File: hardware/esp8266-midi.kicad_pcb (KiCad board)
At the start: 2 copper layers, 62.2 x 63.5 mm, 26 parts, among them J1 MIDI in, J2 MIDI out, J3 TTL-232R-3V3 connector, J4 Bat+, J5 Bat-, SW1 reset, SW2 Prog enable, U1 ESP-12F, U2 6N138, U3 LD1117S50TR_SOT223

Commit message: Initial rev of schematic and PCB, WIP
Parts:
- added C5: 220uF, Capacitors_THT:CP_Radial_D5.0mm_P2.50mm, F.Cu at (125.1, 122.6)
- D1: footprint Diodes_THT:D_DO-41_SOD81_P10.16mm_Horizontal -> Diodes_THT:D_A-405_P10.16mm_Horizontal
- R1, R3, R4, R6: footprint Resistors_THT:R_Axial_DIN0204_L3.6mm_D1.6mm_P7.62mm_Horizontal -> Resistors_THT:R_Axial_DIN0207_L6.3mm_D2.5mm_P10.16mm_Horizontal
- R2, R5: value 430R -> 220R; footprint Resistors_THT:R_Axial_DIN0204_L3.6mm_D1.6mm_P7.62mm_Horizontal -> Resistors_THT:R_Axial_DIN0207_L6.3mm_D2.5mm_P10.16mm_Horizontal
- SW2: value Prog enable -> prog enable
- moved SW1 17.9 mm to (153.0, 128.9), turned to 180 degrees
- moved mount 11.4 mm to (136.5, 84.5)
- moved SW2 10.2 mm to (135.9, 124.5)
- moved R2 3.56 mm to (138.4, 90.2)
- moved D1 1.55 mm to (124.5, 89.5)
- moved R4 1.53 mm to (114.3, 104.1), turned to 90 degrees
- moved R3 0.92 mm to (120.7, 104.1)
- moved R1 0.80 mm to (111.8, 89.5)
- moved R5 0.18 mm to (153.0, 90.2)
- renumbered REF** to mount
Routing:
- net Net-(C1-Pad2): track 52.9 -> 38.2 mm, vias 0 -> 1
- net Net-(SW2-Pad1): track 47.0 -> 32.8 mm, vias 0 -> 1
- net Net-(C2-Pad1): track 15.2 -> 25.1 mm
- net Net-(R4-Pad2): track 2.54 -> 11.3 mm
- net Net-(J2-Pad4): track 6.06 -> 9.44 mm
- net Net-(J2-Pad5): track 5.96 -> 9.04 mm
- net Net-(J1-Pad4): track 5.81 -> 7.80 mm
- net Net-(R3-Pad1): track 23.7 -> 23.0 mm
- added copper zone on B.Cu, net GND
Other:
- board text added: "GND CTS VCC TXD RXD RTS"

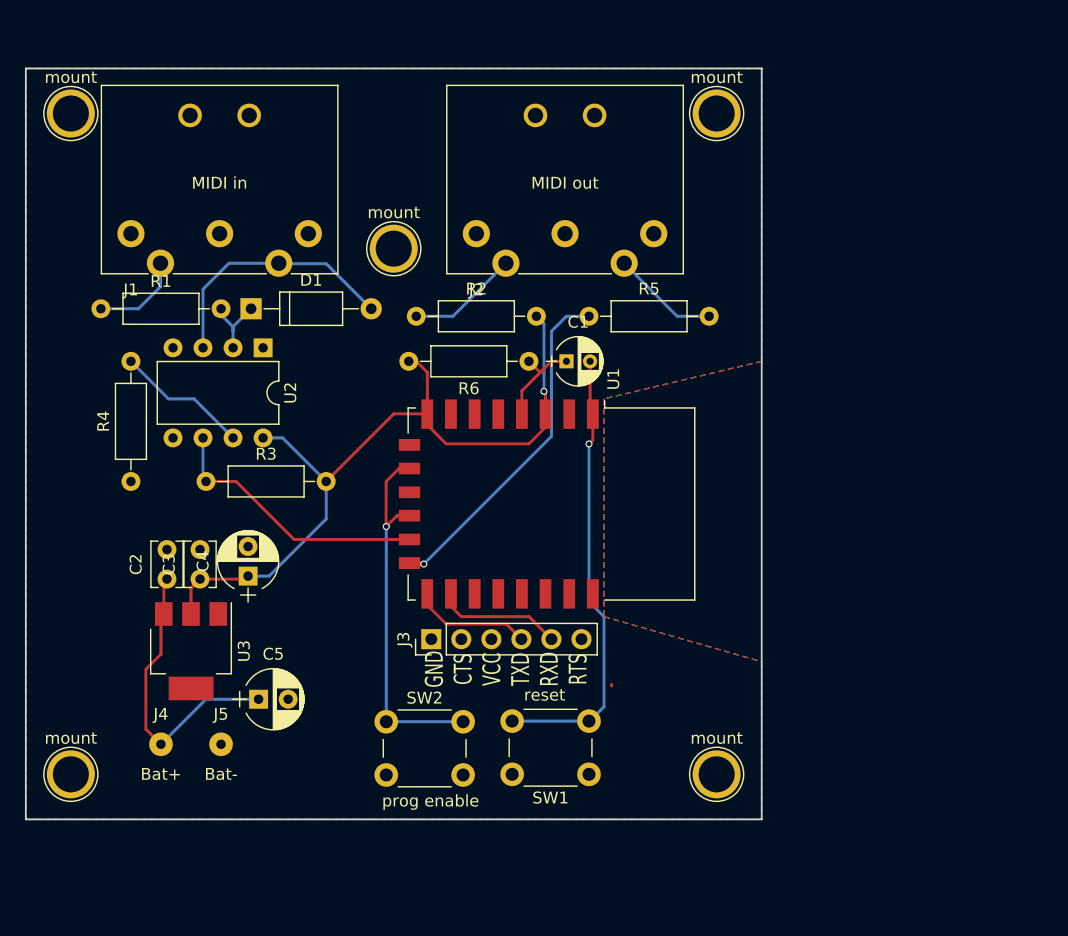
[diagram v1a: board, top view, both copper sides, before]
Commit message: Updated PCB using correct ESP-12E footprint
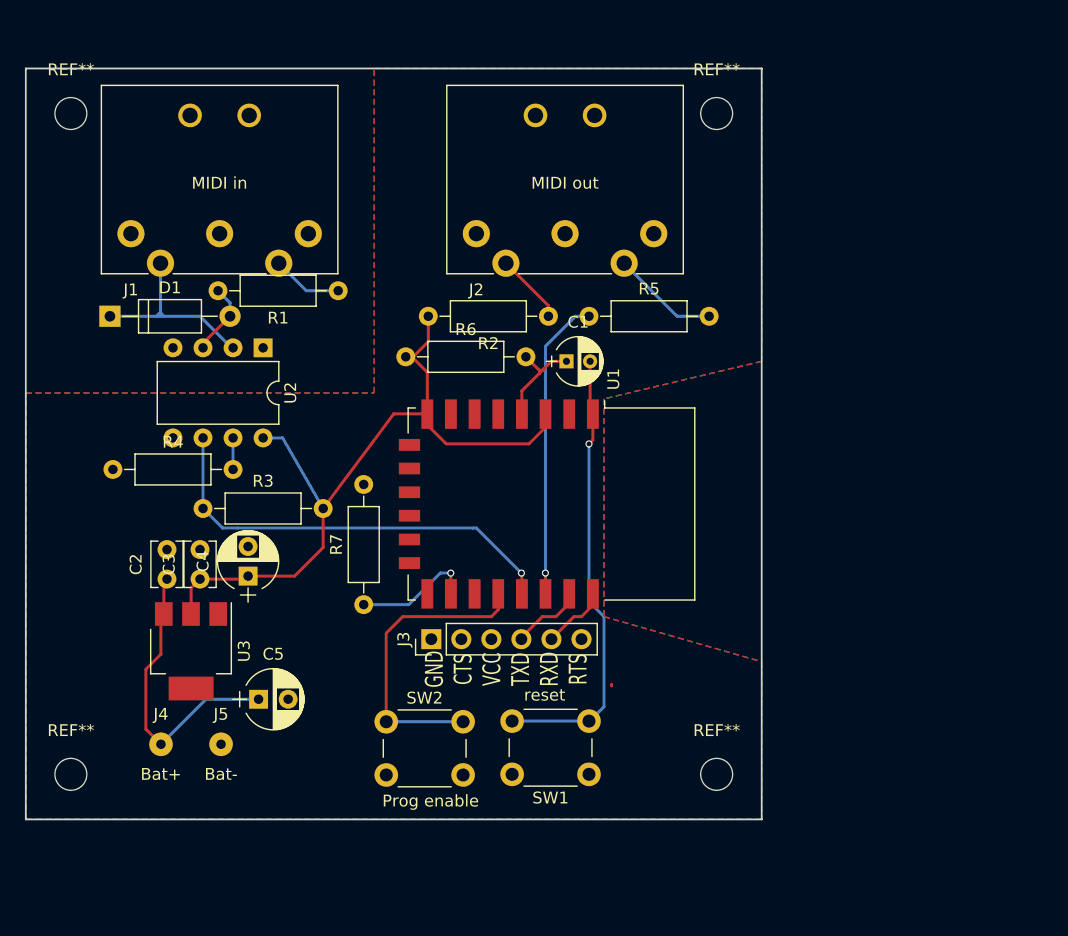
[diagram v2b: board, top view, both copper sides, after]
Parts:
- removed mount (x5): 1pin, Connectors:1pin
- added R7: 10K, Resistors_THT:R_Axial_DIN0207_L6.3mm_D2.5mm_P10.16mm_Horizontal, F.Cu at (134.0, 114.6)
- added REF**: M2.5, Mounting_Holes:MountingHole_2.7mm_M2.5, F.Cu at (163.8, 73.0)
- added REF**: M2.5, Mounting_Holes:MountingHole_2.7mm_M2.5, F.Cu at (163.8, 128.9)
- added REF**: M2.5, Mounting_Holes:MountingHole_2.7mm_M2.5, F.Cu at (109.2, 73.0)
- added REF**: M2.5, Mounting_Holes:MountingHole_2.7mm_M2.5, F.Cu at (109.2, 128.9)
- D1: value D -> 1N4148
- SW2: value prog enable -> Prog enable
- U1: value ESP-12F -> ESP-12E
- moved R1 20.1 mm to (131.8, 88.0), turned to 180 degrees
- moved D1 12.0 mm to (112.5, 90.2)
- moved R2 11.2 mm to (149.6, 90.2), turned to 180 degrees
- moved R6 10.4 mm to (137.5, 93.6), turned to 0 degrees
- moved R3 2.30 mm to (120.4, 106.4)
- moved R4 1.83 mm to (112.8, 103.1), turned to 0 degrees
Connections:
- J1 pad 2: GND -> (no net)
- J1 pad 4: Net-(J1-Pad4) -> Net-(D1-Pad1)
- J1 pad 5: Net-(D1-Pad2) -> Net-(J1-Pad5)
- R1 pad 1: Net-(J1-Pad4) -> Net-(J1-Pad5)
- R1 pad 2: Net-(D1-Pad1) -> Net-(D1-Pad2)
- R6 pad 1: Net-(C1-Pad1) -> +3V3
- R6 pad 2: +3V3 -> Net-(C1-Pad1)
- U1 pad 10: Net-(SW2-Pad1) -> (no net)
- U1 pad 12: Net-(SW2-Pad1) -> (no net)
- U1 pad 13: Net-(R3-Pad1) -> (no net)
- U1 pad 14: Net-(R5-Pad1) -> (no net)
- U1 pad 15: Net-(J3-Pad4) -> GND
- U1 pad 16: Net-(J3-Pad5) -> Net-(R7-Pad1)
- U1 pad 18: (no net) -> Net-(SW2-Pad1)
- U1 pad 19: (no net) -> Net-(R3-Pad1)
- U1 pad 20: (no net) -> Net-(R5-Pad1)
- U1 pad 21: (no net) -> Net-(J3-Pad4)
- U1 pad 22: (no net) -> Net-(J3-Pad5)
- U1 pad 9: GND -> (no net)
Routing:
- net Net-(D1-Pad2): track 21.7 -> 6.19 mm
- net Net-(R3-Pad1): track 23.0 -> 36.9 mm, vias 0 -> 1
- net Net-(D1-Pad1): track 6.13 -> 17.3 mm
- net Net-(R7-Pad1): track 0.00 -> 10.9 mm, vias 0 -> 1
- net Net-(R4-Pad2): track 11.3 -> 2.67 mm
- net Net-(J1-Pad4): track 7.80 -> 0.00 mm
- net Net-(SW2-Pad1): track 32.8 -> 25.6 mm, vias 1 -> 0
- net Net-(J1-Pad5): track 0.00 -> 5.99 mm
- net Net-(J3-Pad5): track 10.7 -> 5.65 mm
- net Net-(J3-Pad4): track 10.1 -> 6.17 mm
- net Net-(J2-Pad4): track 9.44 -> 5.97 mm
- net Net-(R5-Pad1): track 29.1 -> 25.9 mm
- net +3V3: track 64.9 -> 63.4 mm, vias 1 -> 0
- net Net-(C1-Pad1): track 8.57 -> 9.33 mm

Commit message: Hopefully fixed layout now
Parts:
- removed R3: 470R, Resistors_THT:R_Axial_DIN0207_L6.3mm_D2.5mm_P10.16mm_Horizontal
- R2, R5: value 220R -> 120R
- moved C4 9.70 mm to (130.0, 104.4)
- moved C5 2.73 mm to (127.8, 122.6)
- moved R6 1.91 mm to (139.4, 93.6)
- moved C3 1.27 mm to (121.4, 112.4)
- moved R5 1.14 mm to (151.9, 90.2)
- moved R4 1.08 mm to (112.8, 104.2)
- moved C1 0.85 mm to (151.9, 93.6)
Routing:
- net +3V3: track 63.4 -> 57.5 mm
- net Net-(C2-Pad1): track 25.1 -> 27.8 mm
- net Net-(R5-Pad1): track 25.9 -> 28.5 mm
- net Net-(C1-Pad1): track 9.33 -> 8.06 mm
- net Net-(U1-Pad19): track 36.9 -> 35.7 mm
- net Net-(J2-Pad5): track 9.04 -> 7.90 mm
- net Net-(R4-Pad2): track 2.67 -> 3.75 mm
- net Net-(C1-Pad2): track 38.2 -> 39.1 mm

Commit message: Before resizing the board a bit
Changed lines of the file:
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@@
     (thickness 1.6)
     (drawings 9)
-    (tracks 114)
+    (tracks 113)
     (zones 0)
     (modules 26)
@@
   (segment (start 147.36 98.445) (end 147.36 95.845) (width 0.25) (layer F.Cu) (net 1))
   (segment (start 147.36 95.845) (end 149.606 93.599) (width 0.25) (layer F.Cu) (net 1))
+  (segment (start 146.535 124.405) (end 153.035 124.405) (width 0.25) (layer F.Cu) (net 2) (status C00000))
   (segment (start 153.36 98.445) (end 153.36 94.131) (width 0.25) (layer F.Cu) (net 2))
   (segment (start 153.36 94.131) (end 153.892 93.599) (width 0.25) (layer F.Cu) (net 2))
@@
   (segment (start 154.305 115.57) (end 153.035 114.3) (width 0.25) (layer B.Cu) (net 2))
   (segment (start 154.305 123.19) (end 154.305 115.57) (width 0.25) (layer B.Cu) (net 2))
-  (segment (start 146.535 124.405) (end 153.035 124.405) (width 0.25) (layer B.Cu) (net 2))
   (segment (start 153.13 98.215) (end 153.36 98.445) (width 0.25) (layer F.Cu) (net 2))
   (segment (start 116.84 126.365) (end 118.999 124.206) (width 0.25) (layer F.Cu) (net 3))
@@
   (segment (start 140.97 100.965) (end 147.574 100.965) (width 0.25) (layer F.Cu) (net 5))
   (segment (start 139.36 99.355) (end 140.97 100.965) (width 0.25) (layer F.Cu) (net 5))
-  (segment (start 147.574 100.965) (end 149.36 99.179) (width 0.25) (layer F.Cu) (net 5) (status 800000))
-  (segment (start 149.36 99.179) (end 149.36 98.445) (width 0.25) (layer F.Cu) (net 5) (status C00000))
+  (segment (start 147.574 100.965) (end 149.36 99.179) (width 0.25) (layer F.Cu) (net 5))
+  (segment (start 149.36 99.179) (end 149.36 98.445) (width 0.25) (layer F.Cu) (net 5))
   (segment (start 139.36 98.445) (end 135.997 98.445) (width 0.25) (layer F.Cu) (net 5))
   (segment (start 135.997 98.445) (end 130.048 104.394) (width 0.25) (layer F.Cu) (net 5))
@@
   (segment (start 139.34 98.425) (end 139.36 98.445) (width 0.25) (layer F.Cu) (net 5))
   (segment (start 139.7 98.105) (end 139.36 98.445) (width 0.25) (layer F.Cu) (net 5))
-  (segment (start 116.9035 89.9795) (end 116.6495 89.9795) (width 0.25) (layer B.Cu) (net 6))
-  (segment (start 116.713 90.043) (end 116.713 89.916) (width 0.25) (layer B.Cu) (net 6))
-  (segment (start 116.6495 89.9795) (end 116.713 90.043) (width 0.25) (layer B.Cu) (net 6))
-  (segment (start 116.8 89.876) (end 116.753 89.876) (width 0.25) (layer B.Cu) (net 6))
-  (segment (start 116.753 89.876) (end 116.713 89.916) (width 0.25) (layer B.Cu) (net 6))
-  (segment (start 116.713 89.916) (end 116.459 90.17) (width 0.25) (layer B.Cu) (net 6))
-  (segment (start 116.8 85.685) (end 116.8 89.876) (width 0.25) (layer B.Cu) (net 6))
-  (segment (start 116.8 89.876) (end 116.9035 89.9795) (width 0.25) (layer B.Cu) (net 6))
-  (segment (start 116.9035 89.9795) (end 117.094 90.17) (width 0.25) (layer B.Cu) (net 6))
+  (segment (start 116.8 89.789) (end 116.8 89.876) (width 0.25) (layer B.Cu) (net 6))
+  (segment (start 116.8 89.876) (end 117.094 90.17) (width 0.25) (layer B.Cu) (net 6))
+  (segment (start 116.8 89.789) (end 116.8 89.829) (width 0.25) (layer B.Cu) (net 6))
+  (segment (start 116.8 89.829) (end 116.459 90.17) (width 0.25) (layer B.Cu) (net 6))
+  (segment (start 116.8 85.685) (end 116.8 89.789) (width 0.25) (layer B.Cu) (net 6))
+  (segment (start 116.8 89.789) (end 116.8 90.17) (width 0.25) (layer B.Cu) (net 6))
+  (segment (start 116.8 90.17) (end 116.84 90.17) (width 0.25) (layer B.Cu) (net 6))
+  (segment (start 116.459 90.17) (end 112.522 90.17) (width 0.25) (layer B.Cu) (net 6) (status 20))
+  (segment (start 117.094 90.17) (end 116.84 90.17) (width 0.25) (layer B.Cu) (net 6))
+  (segment (start 116.84 90.17) (end 116.459 90.17) (width 0.25) (layer B.Cu) (net 6))
+  (segment (start 120.142 90.17) (end 117.094 90.17) (width 0.25) (layer B.Cu) (net 6))
+  (segment (start 122.809 92.837) (end 120.142 90.17) (width 0.25) (layer B.Cu) (net 6))
   (segment (start 122.936 92.837) (end 122.809 92.837) (width 0.25) (layer B.Cu) (net 6))
-  (segment (start 122.809 92.837) (end 120.142 90.17) (width 0.25) (layer B.Cu) (net 6))
-  (segment (start 120.142 90.17) (end 117.094 90.17) (width 0.25) (layer B.Cu) (net 6))
-  (segment (start 117.094 90.17) (end 116.459 90.17) (width 0.25) (layer B.Cu) (net 6))
-  (segment (start 116.459 90.17) (end 112.522 90.17) (width 0.25) (layer B.Cu) (net 6))
-  (segment (start 112.522 90.17) (end 112.522 89.963) (width 0.25) (layer B.Cu) (net 6))
+  (segment (start 112.522 90.17) (end 112.522 89.963) (width 0.25) (layer B.Cu) (net 6) (status 30))
+  (segment (start 121.666 89.154) (end 122.682 90.17) (width 0.25) (layer F.Cu) (net 7) (status 20))
+  (segment (start 120.396 92.456) (end 122.682 90.17) (width 0.25) (layer F.Cu) (net 7) (status 20))
   (segment (start 121.666 88.011) (end 121.666 89.154) (width 0.25) (layer F.Cu) (net 7))
-  (segment (start 121.666 89.154) (end 122.682 90.17) (width 0.25) (layer F.Cu) (net 7))
   (segment (start 120.396 92.837) (end 120.396 92.456) (width 0.25) (layer F.Cu) (net 7))
-  (segment (start 120.396 92.456) (end 122.682 90.17) (width 0.25) (layer F.Cu) (net 7))
   (segment (start 162.052 90.17) (end 160.495 90.17) (width 0.25) (layer F.Cu) (net 8))
   (segment (start 160.495 90.17) (end 156.01 85.685) (width 0.25) (layer F.Cu) (net 8))
@@
   (segment (start 149.36 113.645) (end 149.36 111.895) (width 0.25) (layer F.Cu) (net 13))
   (segment (start 149.36 111.895) (end 149.352 111.887) (width 0.25) (layer F.Cu) (net 13))
+  (segment (start 135.89 124.46) (end 142.39 124.46) (width 0.25) (layer F.Cu) (net 14) (status C00000))
   (segment (start 135.89 124.46) (end 135.89 116.967) (width 0.25) (layer F.Cu) (net 14))
   (segment (start 145.36 114.99) (end 145.36 113.645) (width 0.25) (layer F.Cu) (net 14))
@@
   (segment (start 137.287 115.57) (end 144.78 115.57) (width 0.25) (layer F.Cu) (net 14))
   (segment (start 135.89 116.967) (end 137.287 115.57) (width 0.25) (layer F.Cu) (net 14))
-  (segment (start 142.39 124.46) (end 135.89 124.46) (width 0.25) (layer B.Cu) (net 14) (status 30))
+  (segment (start 129.032 88.011) (end 131.826 88.011) (width 0.25) (layer F.Cu) (net 15))
+  (segment (start 126.8 85.779) (end 129.032 88.011) (width 0.25) (layer F.Cu) (net 15))
   (segment (start 126.8 85.685) (end 126.8 85.779) (width 0.25) (layer F.Cu) (net 15))
-  (segment (start 126.8 85.779) (end 129.032 88.011) (width 0.25) (layer F.Cu) (net 15))
-  (segment (start 129.032 88.011) (end 131.826 88.011) (width 0.25) (layer F.Cu) (net 15))
   (segment (start 133.985 114.554) (end 137.795 114.554) (width 0.25) (layer B.Cu) (net 16))
   (segment (start 141.36 111.896) (end 141.36 113.645) (width 0.25) (layer F.Cu) (net 16))
@@
   (segment (start 141.36 114.291) (end 141.36 113.645) (width 0.25) (layer F.Cu) (net 16))
   (segment (start 124.206 108.077) (end 143.51 108.077) (width 0.25) (layer B.Cu) (net 17))
-  (segment (start 120.396 100.457) (end 120.396 104.267) (width 0.25) (layer B.Cu) (net 17) (status 400000))
+  (segment (start 120.396 100.457) (end 120.396 104.267) (width 0.25) (layer B.Cu) (net 17))
   (segment (start 124.206 108.077) (end 120.396 104.267) (width 0.25) (layer B.Cu) (net 17))
   (segment (start 147.36 111.927) (end 147.36 113.645) (width 0.25) (layer F.Cu) (net 17))

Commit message: Small resize of the board + relocating some stuff + some rounded ground zone corners
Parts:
- SW2: value Prog enable -> prog enable
- moved mount 2.16 mm to (161.7, 73.0)
- moved mount 2.16 mm to (161.7, 128.9)
- moved R2 2.16 mm to (147.4, 90.2)
- moved R6 2.16 mm to (137.3, 93.6)
- moved J2 1.91 mm to (141.6, 83.2)
- moved R5 1.78 mm to (150.1, 90.2)
- moved C1 0.63 mm to (151.3, 93.6)
- renumbered REF** to mount
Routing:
- net Net-(R5-Pad1): track 28.5 -> 24.0 mm
- net +3V3: track 57.5 -> 58.3 mm
- net Net-(C1-Pad1): track 8.06 -> 8.69 mm
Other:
- board size 62.2 x 63.5 mm -> 60.1 x 63.5 mm
